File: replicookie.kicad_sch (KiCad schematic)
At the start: 0 parts

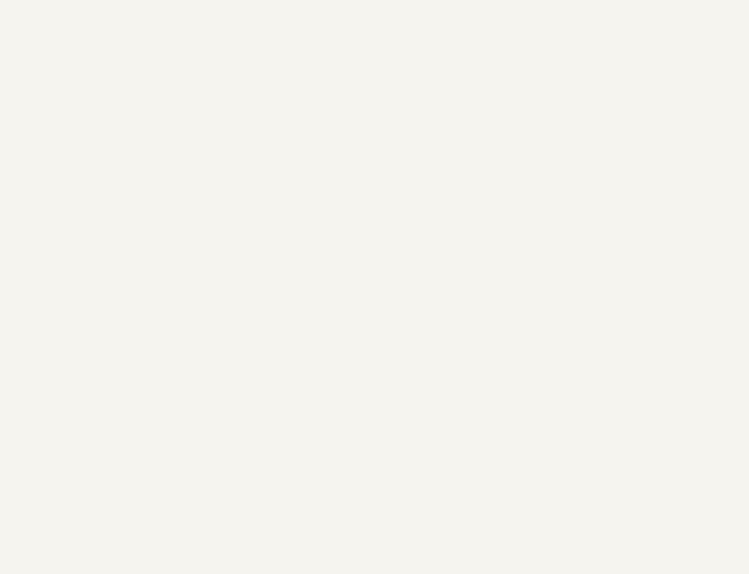
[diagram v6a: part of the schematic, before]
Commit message: Expand PCB, change to inches, center Snickerdoodle
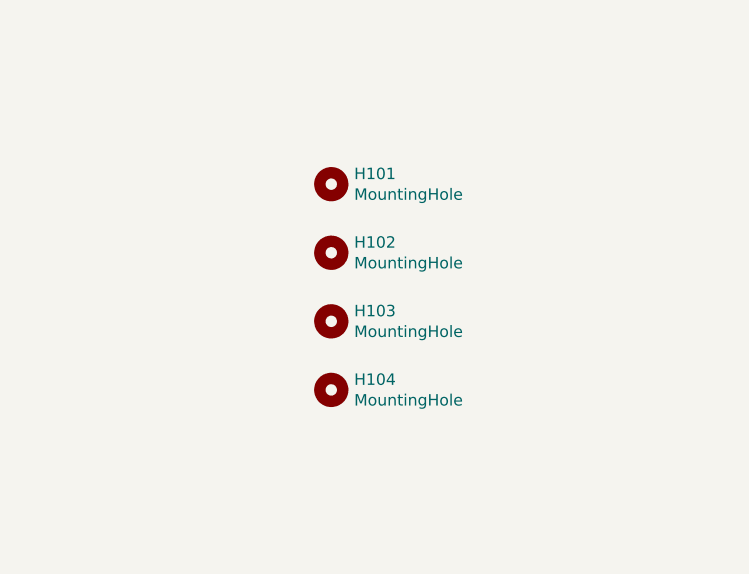
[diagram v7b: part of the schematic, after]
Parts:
- added H101, H102, H103, H104: MountingHole, MountingHole:MountingHole_3mm, symbol Mechanical:MountingHole
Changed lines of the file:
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@@
-(kicad_sch (version 20200714) (host eeschema "5.99.0-unknown-9b6ade6b1~102~ubuntu20.04.1")
+(kicad_sch (version 20200714) (host eeschema "5.99.0-unknown-829316fad~102~ubuntu20.04.1")
   (page 1 15)
   (paper "B")
@@
     (effects (font (size 1.27 1.27)) (justify right bottom))
   )
+  (symbol (lib_id "Mechanical:MountingHole") (at 330.2 179.07 0) (unit 1)
+    (in_bom yes) (on_board yes)
+    (property "Reference" "H101" (id 0) (at 332.7401 177.9206 0)
+      (effects (font (size 1.27 1.27)) (justify left))
+    )
+    (property "Value" "MountingHole" (id 1) (at 332.7401 180.2193 0)
+      (effects (font (size 1.27 1.27)) (justify left))
+    )
+    (property "Footprint" "MountingHole:MountingHole_3mm" (id 2) (at 330.2 179.07 0)
+      (effects (font (size 1.27 1.27)) hide)
+    )
+    (property "Datasheet" "~" (id 3) (at 330.2 179.07 0)
+      (effects (font (size 1.27 1.27)) hide)
+    )
+  )
+  (symbol (lib_id "Mechanical:MountingHole") (at 330.2 186.69 0) (unit 1)
+    (in_bom yes) (on_board yes)
+    (property "Reference" "H102" (id 0) (at 332.7401 185.5406 0)
+      (effects (font (size 1.27 1.27)) (justify left))
+    )
+    (property "Value" "MountingHole" (id 1) (at 332.7401 187.8393 0)
+      (effects (font (size 1.27 1.27)) (justify left))
+    )
+    (property "Footprint" "MountingHole:MountingHole_3mm" (id 2) (at 330.2 186.69 0)
+      (effects (font (size 1.27 1.27)) hide)
+    )
+    (property "Datasheet" "~" (id 3) (at 330.2 186.69 0)
+      (effects (font (size 1.27 1.27)) hide)
+    )
+  )
+  (symbol (lib_id "Mechanical:MountingHole") (at 330.2 194.31 0) (unit 1)
+    (in_bom yes) (on_board yes)
+    (property "Reference" "H103" (id 0) (at 332.7401 193.1606 0)
+      (effects (font (size 1.27 1.27)) (justify left))
+    )
+    (property "Value" "MountingHole" (id 1) (at 332.7401 195.4593 0)
+      (effects (font (size 1.27 1.27)) (justify left))
+    )
+    (property "Footprint" "MountingHole:MountingHole_3mm" (id 2) (at 330.2 194.31 0)
+      (effects (font (size 1.27 1.27)) hide)
+    )
+    (property "Datasheet" "~" (id 3) (at 330.2 194.31 0)
+      (effects (font (size 1.27 1.27)) hide)
+    )
+  )
+  (symbol (lib_id "Mechanical:MountingHole") (at 330.2 201.93 0) (unit 1)
+    (in_bom yes) (on_board yes)
+    (property "Reference" "H104" (id 0) (at 332.7401 200.7806 0)
+      (effects (font (size 1.27 1.27)) (justify left))
+    )
+    (property "Value" "MountingHole" (id 1) (at 332.7401 203.0793 0)
+      (effects (font (size 1.27 1.27)) (justify left))
+    )
+    (property "Footprint" "MountingHole:MountingHole_3mm" (id 2) (at 330.2 201.93 0)
+      (effects (font (size 1.27 1.27)) hide)
+    )
+    (property "Datasheet" "~" (id 3) (at 330.2 201.93 0)
+      (effects (font (size 1.27 1.27)) hide)
+    )
+  )
   (sheet (at 76.2 124.46) (size 25.4 13.97)
     (stroke (width 0.0006) (type solid) (color 132 0 132 1))
@@
   )
   (symbol_instances
+    (path "/4fcb72b1-94ad-4f9e-a1b6-871b6bdaf265"
+      (reference "H101") (unit 1)
+    )
+    (path "/79e38670-fe99-47dd-b318-626db112cfbe"
+      (reference "H102") (unit 1)
+    )
+    (path "/220912b1-38f2-416c-97a4-1b7da36758e6"
+      (reference "H103") (unit 1)
+    )
+    (path "/61c1711c-87e8-499d-84a4-2912eb77474d"
+      (reference "H104") (unit 1)
+    )
     (path "/655846c9-6d11-4b61-aecf-3ea94510aa57/a31059e0-2106-4ba5-9ab1-2330ed94e840"
       (reference "#PWR0201") (unit 1)
@@
       (reference "#PWR0315") (unit 1)
     )
-    (path "/b7ae1606-d3c7-49bb-8bec-a97be30f1474/1eb3edb7-c24e-4257-a7cb-9d9790ff9b32"
-      (reference "#PWR0316") (unit 1)
-    )
     (path "/b7ae1606-d3c7-49bb-8bec-a97be30f1474/c23447e9-6a50-4056-9567-1f3529286499"
       (reference "#PWR0317") (unit 1)
@@
       (reference "R307") (unit 1)
     )
-    (path "/b7ae1606-d3c7-49bb-8bec-a97be30f1474/624de630-9813-478e-83b0-cfacbf331f59"
-      (reference "R308") (unit 1)
-    )
-    (path "/b7ae1606-d3c7-49bb-8bec-a97be30f1474/925c9630-7fd5-4ae3-9bdc-a3ec73f948d2"
-      (reference "R309") (unit 1)
-    )
     (path "/b7ae1606-d3c7-49bb-8bec-a97be30f1474/4e4da4ed-3360-4dd7-a008-abd97309b8b4"
